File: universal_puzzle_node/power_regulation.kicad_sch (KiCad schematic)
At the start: 8 parts

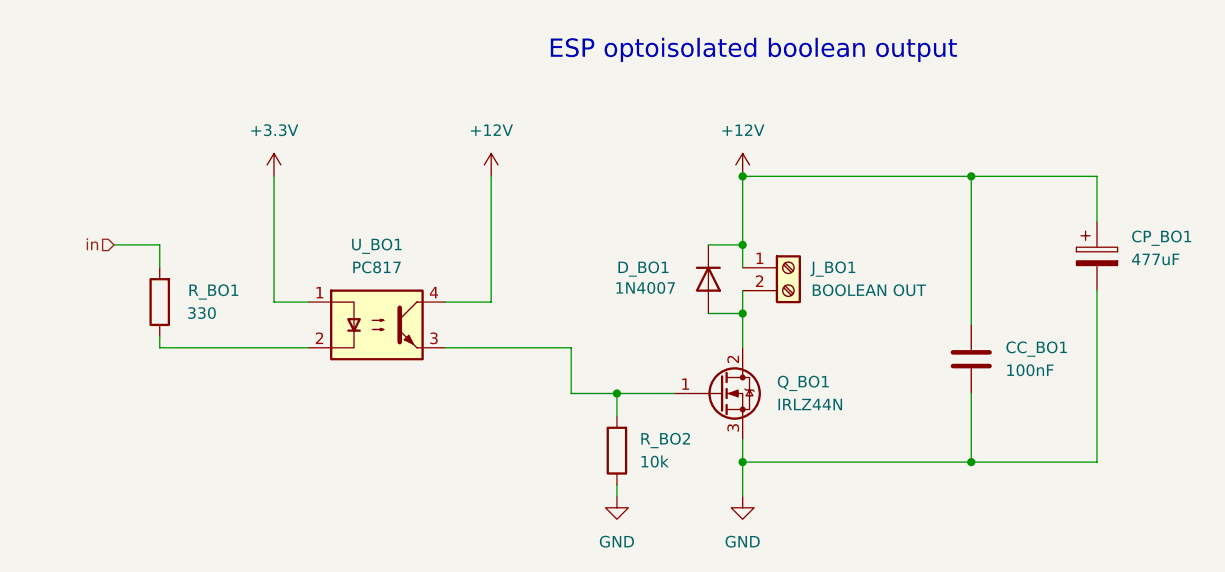
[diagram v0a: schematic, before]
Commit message: chore: rename to universal puzzle node everywhere
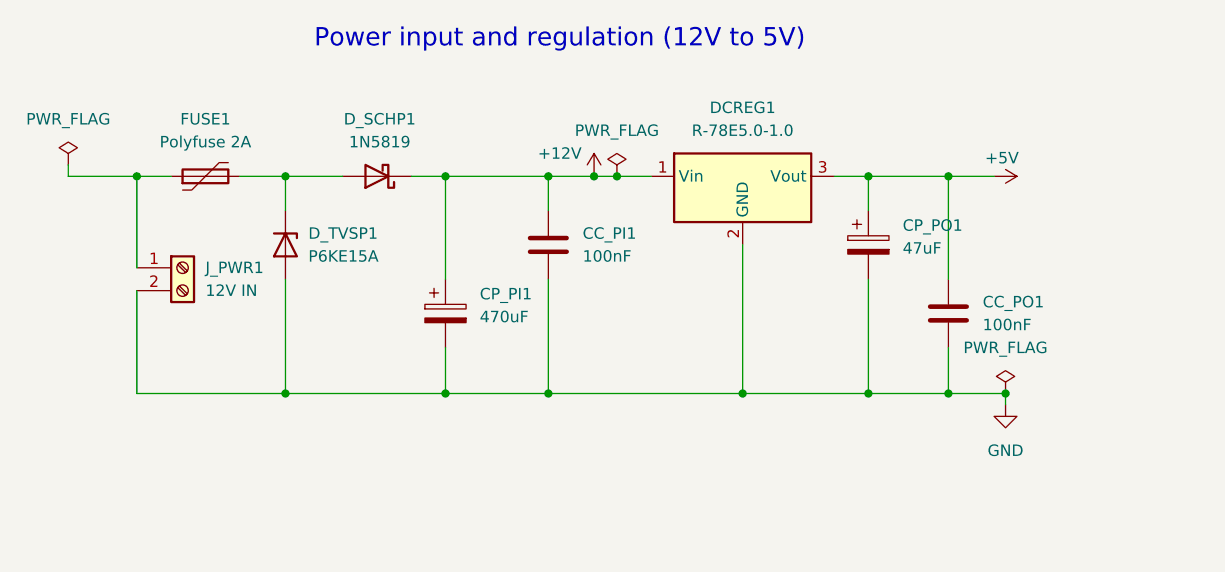
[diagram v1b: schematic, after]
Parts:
- removed CC_BO1: 100nF, Capacitor_THT:C_Disc_D5.0mm_W2.5mm_P5.00mm, symbol Device:C
- removed CP_BO1: 477uF, Capacitor_THT:CP_Radial_D10.0mm_P5.00mm, symbol Device:C_Polarized
- removed D_BO1: 1N4007, Diode_THT:D_DO-41_SOD81_P10.16mm_Horizontal, symbol Diode:1N4007
- removed J_BO1: BOOLEAN OUT, TerminalBlock_Phoenix:TerminalBlock_Phoenix_MKDS-1,5-2-5.08_1x02_P5.08mm_Horizontal, symbol Connector:Screw_Terminal_01x02
- removed Q_BO1: IRLZ44N, Package_TO_SOT_THT:TO-220-3_Vertical, symbol Transistor_FET:IRLZ44N
- removed R_BO1: 330, Resistor_THT:R_Axial_DIN0207_L6.3mm_D2.5mm_P10.16mm_Horizontal, symbol Device:R
- removed R_BO2: 10k, Resistor_THT:R_Axial_DIN0207_L6.3mm_D2.5mm_P10.16mm_Horizontal, symbol Device:R
- removed U_BO1: PC817, Package_DIP:DIP-4_W7.62mm, symbol Isolator:PC817
- added CC_PI1, CC_PO1: 100nF, Capacitor_THT:C_Disc_D5.0mm_W2.5mm_P5.00mm, symbol Device:C
- added CP_PI1: 470uF, Capacitor_THT:CP_Radial_D10.0mm_P5.00mm, symbol Device:C_Polarized
- added CP_PO1: 47uF, Capacitor_THT:CP_Radial_D6.3mm_P2.50mm, symbol Device:C_Polarized
- added DCREG1: R-78E5.0-1.0, Converter_DCDC:Converter_DCDC_RECOM_R-78E-0.5_THT, symbol Converter_DCDC:TSR2-2450
- added D_SCHP1: 1N5819, Diode_THT:D_DO-35_SOD27_P7.62mm_Horizontal, symbol Device:D_Schottky
- added D_TVSP1: P6KE15A, Diode_THT:D_DO-15_P12.70mm_Horizontal, symbol Diode:PTVS15VZ1USK
- added FUSE1: Polyfuse 2A, Fuse:Fuse_BelFuse_0ZRE0040FF_L11.5mm_W3.8mm, symbol Device:Polyfuse
- added J_PWR1: 12V IN, TerminalBlock_Phoenix:TerminalBlock_Phoenix_MKDS-1,5-2-5.08_1x02_P5.08mm_Horizontal, symbol Connector:Screw_Terminal_01x02
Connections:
- net +12V: now also CC_PI1.1, CP_PI1.1, DCREG1.1 (Vin), D_SCHP1.1 (K)
- net GND: now also CC_PI1.2, CC_PO1.2, CP_PI1.2, CP_PO1.2, DCREG1.2 (GND), D_TVSP1.2 (A), J_PWR1.2 (Pin_2)
- new net: D_SCHP1.2 (A), D_TVSP1.1 (K), FUSE1.2
- new net: FUSE1.1, J_PWR1.1 (Pin_1)
- new net +5V: CC_PO1.1, CP_PO1.1, DCREG1.3 (Vout)
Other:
- note added: "Power input and regulation (12V to 5V)"
- note removed: "ESP optoisolated boolean output"
- title: ESP optoisolated boolean input -> Power input and regulation
